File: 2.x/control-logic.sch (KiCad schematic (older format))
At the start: 37 parts, among them P7 SWD, P8 FTDI_SERIAL, SW1 DIPS_08, SW2 RESET, SW3 BOOTLOADER, U2 74HC595, U3 74HC595, U4 LPC11C22FBD48/301, U5 74HC165, X1 12.000 MHz

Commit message: Added RGB output and finished power supply monitor schematic, including new current monitor and voltage monitor divider values.
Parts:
- D33: value HEARTBEAT -> LED
- D34: value POWER_GOOD -> LED
- SW2: value RESET -> BUTTON
- SW3: value BOOTLOADER -> BUTTON
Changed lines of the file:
@@
 $Descr USLetter 11000 8500
 encoding utf-8
-Sheet 5 6
-Title ""
+Sheet 5 7
+Title "DIYPinball Base Board"
 Date "17 mar 2014"
-Rev ""
-Comp ""
+Rev "2.0"
+Comp "DIYPinball.ca"
 Comment1 ""
 Comment2 ""
@@
 SOLENOID_LAMP_LAT
 $Comp
-L GND #PWR28
+L GND #PWR29
 U 1 1 5325ACE0
 P 2800 7550
-F 0 "#PWR28" H 2800 7550 30  0001 C CNN
+F 0 "#PWR29" H 2800 7550 30  0001 C CNN
 F 1 "GND" H 2800 7480 30  0001 C CNN
 F 2 "" H 2800 7550 60  0000 C CNN
@@
 $EndComp
 $Comp
-L GND #PWR32
+L GND #PWR33
 U 1 1 5325BA22
 P 7350 7050
-F 0 "#PWR32" H 7350 7050 30  0001 C CNN
+F 0 "#PWR33" H 7350 7050 30  0001 C CNN
 F 1 "GND" H 7350 6980 30  0001 C CNN
 F 2 "" H 7350 7050 60  0000 C CNN
@@
 VSOL_PRECHARGE_PWM
 $Comp
-L GND #PWR29
+L GND #PWR30
 U 1 1 53262BD9
 P 3650 4200
-F 0 "#PWR29" H 3650 4200 30  0001 C CNN
+F 0 "#PWR30" H 3650 4200 30  0001 C CNN
 F 1 "GND" H 3650 4130 30  0001 C CNN
 F 2 "" H 3650 4200 60  0000 C CNN
@@
 $EndComp
 $Comp
-L GND #PWR31
+L GND #PWR32
 U 1 1 53267486
 P 5350 7850
-F 0 "#PWR31" H 5350 7850 30  0001 C CNN
+F 0 "#PWR32" H 5350 7850 30  0001 C CNN
 F 1 "GND" H 5350 7780 30  0001 C CNN
 F 2 "" H 5350 7850 60  0000 C CNN
@@
 P 8050 2400
 F 0 "SW2" H 8200 2510 50  0000 C CNN
-F 1 "RESET" H 8050 2320 50  0000 C CNN
+F 1 "BUTTON" H 8050 2320 50  0000 C CNN
 F 2 "~" H 8050 2400 60  0000 C CNN
 F 3 "~" H 8050 2400 60  0000 C CNN
@@
 P 8500 2400
 F 0 "SW3" H 8650 2510 50  0000 C CNN
-F 1 "BOOTLOADER" H 8500 2320 50  0000 C CNN
+F 1 "BUTTON" H 8500 2320 50  0000 C CNN
 F 2 "~" H 8500 2400 60  0000 C CNN
 F 3 "~" H 8500 2400 60  0000 C CNN
@@
 P 10100 1900
 F 0 "D34" H 10100 2000 50  0000 C CNN
-F 1 "POWER_GOOD" H 10100 1800 50  0000 C CNN
+F 1 "LED" H 10100 1800 50  0000 C CNN
 F 2 "~" H 10100 1900 60  0000 C CNN
 F 3 "~" H 10100 1900 60  0000 C CNN
@@
 P 9800 1900
 F 0 "D33" H 9800 2000 50  0000 C CNN
-F 1 "HEARTBEAT" H 9800 1800 50  0000 C CNN
+F 1 "LED" H 9800 1800 50  0000 C CNN
 F 2 "~" H 9800 1900 60  0000 C CNN
 F 3 "~" H 9800 1900 60  0000 C CNN
@@
 $EndComp
 $Comp
-L GND #PWR30
+L GND #PWR31
 U 1 1 53268402
 P 4150 4700
-F 0 "#PWR30" H 4150 4700 30  0001 C CNN
+F 0 "#PWR31" H 4150 4700 30  0001 C CNN
 F 1 "GND" H 4150 4630 30  0001 C CNN
 F 2 "" H 4150 4700 60  0000 C CNN
@@
 LOCAL_3V3
 $Comp
-L GND #PWR34
+L GND #PWR35
 U 1 1 53268FE5
 P 8050 2900
-F 0 "#PWR34" H 8050 2900 30  0001 C CNN
+F 0 "#PWR35" H 8050 2900 30  0001 C CNN
 F 1 "GND" H 8050 2830 30  0001 C CNN
 F 2 "" H 8050 2900 60  0000 C CNN
@@
 LOCAL_3V3
 $Comp
-L GND #PWR35
+L GND #PWR36
 U 1 1 532697A4
 P 9950 2900
-F 0 "#PWR35" H 9950 2900 30  0001 C CNN
+F 0 "#PWR36" H 9950 2900 30  0001 C CNN
 F 1 "GND" H 9950 2830 30  0001 C CNN
 F 2 "" H 9950 2900 60  0000 C CNN
@@
 POWER_GOOD
 $Comp
-L GND #PWR33
+L GND #PWR34
 U 1 1 5326A151
 P 7850 3750
-F 0 "#PWR33" H 7850 3750 30  0001 C CNN
+F 0 "#PWR34" H 7850 3750 30  0001 C CNN
 F 1 "GND" H 7850 3680 30  0001 C CNN
 F 2 "" H 7850 3750 60  0000 C CNN
@@
 TXD
 $Comp
-L GND #PWR36
+L GND #PWR37
 U 1 1 5326B790
 P 10000 3750
-F 0 "#PWR36" H 10000 3750 30  0001 C CNN
+F 0 "#PWR37" H 10000 3750 30  0001 C CNN
 F 1 "GND" H 10000 3680 30  0001 C CNN
 F 2 "" H 10000 3750 60  0000 C CNN
@@
 $EndComp
 $Comp
-L GND #PWR?
+L GND #PWR28
 U 1 1 53272581
 P 2800 6150
-F 0 "#PWR?" H 2800 6150 30  0001 C CNN
+F 0 "#PWR28" H 2800 6150 30  0001 C CNN
 F 1 "GND" H 2800 6080 30  0001 C CNN
 F 2 "" H 2800 6150 60  0000 C CNN

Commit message: Adding I2C connector and reannotating to reflect that
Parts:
- added P9: CONN_4, symbol CONN_4
- added R139, R140: 4K7, ~, symbol R
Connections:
- wire segments 198 -> 208
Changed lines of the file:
@@
 Sheet 5 7
 Title "DIYPinball Base Board"
-Date "17 mar 2014"
+Date "2 apr 2014"
 Rev "2.0"
 Comp "DIYPinball.ca"
@@
 LOCAL_3V3
 $Comp
-L GND #PWR36
+L GND #PWR37
 U 1 1 532697A4
 P 9950 2900
-F 0 "#PWR36" H 9950 2900 30  0001 C CNN
+F 0 "#PWR37" H 9950 2900 30  0001 C CNN
 F 1 "GND" H 9950 2830 30  0001 C CNN
 F 2 "" H 9950 2900 60  0000 C CNN
@@
 TXD
 $Comp
-L GND #PWR37
+L GND #PWR38
 U 1 1 5326B790
 P 10000 3750
-F 0 "#PWR37" H 10000 3750 30  0001 C CNN
+F 0 "#PWR38" H 10000 3750 30  0001 C CNN
 F 1 "GND" H 10000 3680 30  0001 C CNN
 F 2 "" H 10000 3750 60  0000 C CNN
@@
 Wire Wire Line
 	1500 2950 2550 2950
+$Comp
+L CONN_4 P9
+U 1 1 533CA25E
+P 9550 4550
+F 0 "P9" V 9500 4550 50  0000 C CNN
+F 1 "CONN_4" V 9600 4550 50  0000 C CNN
+F 2 "" H 9550 4550 60  0000 C CNN
+F 3 "" H 9550 4550 60  0000 C CNN
+	1    9550 4550
+	1    0    0    -1
+$EndComp
+Text Label 8400 4000 0    60   ~ 0
+LOCAL_3V3
+Text Label 8400 4600 0    60   ~ 0
+SCL
+Text Label 8400 4700 0    60   ~ 0
+SDA
+Wire Wire Line
+	8400 4700 9200 4700
+Wire Wire Line
+	9200 4600 8400 4600
+Wire Wire Line
+	8400 4000 9200 4000
+$Comp
+L GND #PWR36
+U 1 1 533CA56F
+P 9100 4800
+F 0 "#PWR36" H 9100 4800 30  0001 C CNN
+F 1 "GND" H 9100 4730 30  0001 C CNN
+F 2 "" H 9100 4800 60  0000 C CNN
+F 3 "" H 9100 4800 60  0000 C CNN
+	1    9100 4800
+	1    0    0    -1
+$EndComp
+Wire Wire Line
+	9100 4800 9100 4500
+Wire Wire Line
+	9100 4500 9200 4500
+Wire Wire Line
+	9200 4000 9200 4400
+$Comp
+L R R140
+U 1 1 533CAC4E
+P 8950 4300
+F 0 "R140" V 9030 4300 40  0000 C CNN
+F 1 "4K7" V 8957 4301 40  0000 C CNN
+F 2 "~" V 8880 4300 30  0000 C CNN
+F 3 "~" H 8950 4300 30  0000 C CNN
+	1    8950 4300
+	1    0    0    -1
+$EndComp
+$Comp
+L R R139
+U 1 1 533CAE0E
+P 8750 4300
+F 0 "R139" V 8830 4300 40  0000 C CNN
+F 1 "4K7" V 8757 4301 40  0000 C CNN
+F 2 "~" V 8680 4300 30  0000 C CNN
+F 3 "~" H 8750 4300 30  0000 C CNN
+	1    8750 4300
+	1    0    0    -1
+$EndComp
+Wire Wire Line
+	8750 4550 8750 4600
+Connection ~ 8750 4600
+Wire Wire Line
+	8950 4550 8950 4700
+Connection ~ 8950 4700
+Wire Wire Line
+	8950 4050 8950 4000
+Connection ~ 8950 4000
+Wire Wire Line
+	8750 4050 8750 4000
+Connection ~ 8750 4000
 $EndSCHEMATC

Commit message: Cleaning up schematic Updating solenoid driver to use 12V for MOSFET gates instead of Vsol so we never exceed Vgs_max
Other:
- moved on the sheet: C10, C12, C14, D33, D34, P8, P9, R103, R104, R105, R106, R107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

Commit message: Started layout on 2.0
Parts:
- removed C10, C13, C14: 100n, ~, symbol C
- removed P7: SWD, symbol CONN_5X2
- removed R101, R102: 10K, ~, symbol R
- removed U2, U3: 74HC595, ~, symbol 74HC595
- removed U4: LPC11C22FBD48/301, symbol LPC11C22FBD48/301
- removed U5: 74HC165, ~, symbol 74LS165
- added C11: 100n, Capacitors_SMD:C_0603, symbol C
- added PGM1: ARM-SWD-HEADER, Myelin:pin_array_5x2_50mil_smd, symbol ARM-SWD-HEADER
- added U2: STM32F072R, Housings_QFP:LQFP-64_10x10mm_Pitch0.5mm, symbol STM32F072R
- added U3: MCP2562, Housings_SOIC:SOIC-8_3.9x4.9mm_Pitch1.27mm, symbol MCP2562
- ADR1: renamed from SW1; footprint (none) -> PinballParts:DIPSWITCH-SMT-08
- BOOT1: renamed from SW3; footprint ~ -> Buttons_Switches_ThroughHole:SW_PUSH_SMALL
- C10: renamed from C11; footprint ~ -> Capacitors_SMD:C_0603
- C12, C4, C5, C6, C7, C8, C9: footprint ~ -> Capacitors_SMD:C_0603
- HB1: renamed from D33; footprint ~ -> LEDs:LED-0603
- I2C1: renamed from P9; footprint (none) -> Sockets_MOLEX_KK-System:Socket_MOLEX-KK-RM2-54mm_Lock_4pin_straight
- PG1: renamed from D34; footprint ~ -> LEDs:LED-0603
- R101: renamed from R111; footprint ~ -> Resistors_SMD:R_0603
- R102: renamed from R112; footprint ~ -> Resistors_SMD:R_0603
- R103: renamed from R113; footprint ~ -> Resistors_SMD:R_0603
- R104: renamed from R114; footprint ~ -> Resistors_SMD:R_0603
- R105: renamed from R139; value 4K7 -> 4.7K; footprint ~ -> Resistors_SMD:R_0603
- R106: renamed from R140; value 4K7 -> 4.7K; footprint ~ -> Resistors_SMD:R_0603
- R107: renamed from R103; footprint ~ -> Resistors_SMD:R_0603
- R108: renamed from R104; footprint ~ -> Resistors_SMD:R_0603
- R109: renamed from R105; footprint ~ -> Resistors_SMD:R_0603
- R110: renamed from R106; footprint ~ -> Resistors_SMD:R_0603
- R111: renamed from R107; footprint ~ -> Resistors_SMD:R_0603
- R112: renamed from R108; footprint ~ -> Resistors_SMD:R_0603
- R113: renamed from R109; footprint ~ -> Resistors_SMD:R_0603
- R114: renamed from R110; footprint ~ -> Resistors_SMD:R_0603
- RESET1: renamed from SW2; footprint ~ -> Buttons_Switches_ThroughHole:SW_PUSH_SMALL
- SERIAL1: renamed from P8; footprint (none) -> Socket_Strips:Socket_Strip_Straight_1x06
- X1: value 12.000 MHz -> 8.000 MHz; footprint ~ -> Crystals_Oscillators_SMD:Q_49U3HMS
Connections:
- net labels added: ADDRESS0, ADDRESS1, ADDRESS2, ADDRESS3, ADDRESS4, ADDRESS5, ADDRESS6, ADDRESS7, CANRX, CANTX, ~RESET
- net labels removed: DIP_CLK, DIP_DAT, DIP_LAT, RESET, SOLENOID_LAMP_CLEAR, SOLENOID_LAMP_CLK, SOLENOID_LAMP_DAT, SOLENOID_LAMP_LAT
- wire segments 208 -> 188
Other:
- moved on the sheet: ADR1, C10, C4, C5, C6, C7, C8, C9, R107, R108, R109, R110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

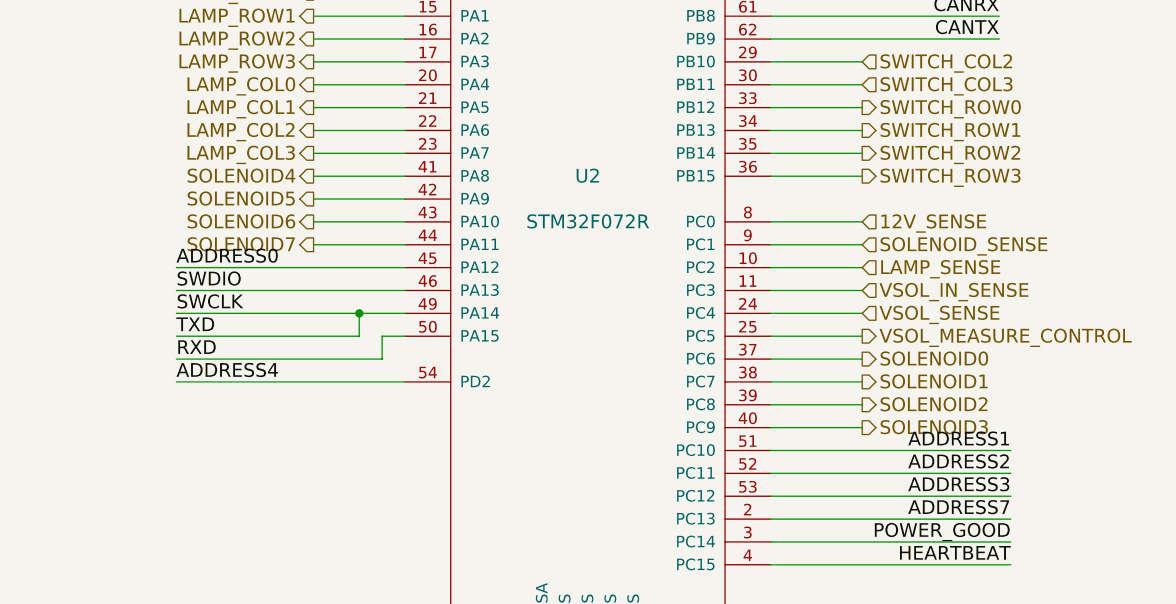
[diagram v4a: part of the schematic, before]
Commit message: 2.0 is getting very close. Adjusted the solenoid connections to allow a cleaner layout.
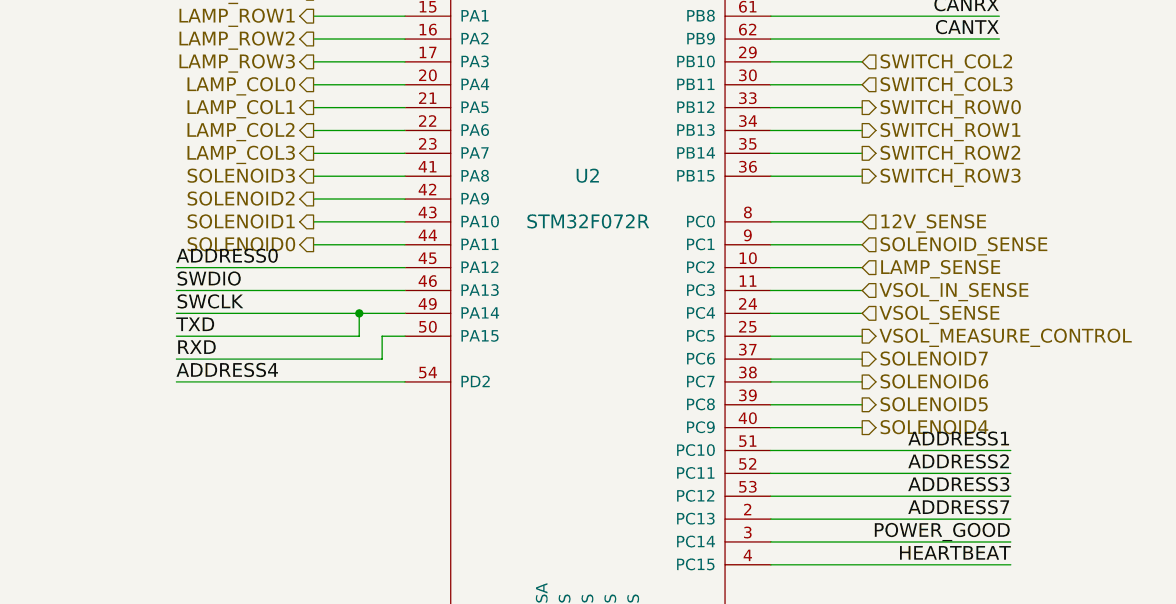
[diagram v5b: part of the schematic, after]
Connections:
- net SOLENOID0: now also U2.44 (PA11); no longer U2.37 (PC6)
- net SOLENOID1: now also U2.43 (PA10); no longer U2.38 (PC7)
- net SOLENOID2: now also U2.42 (PA9); no longer U2.39 (PC8)
- net SOLENOID3: now also U2.41 (PA8); no longer U2.40 (PC9)
- net SOLENOID4: now also U2.40 (PC9); no longer U2.41 (PA8)
- net SOLENOID5: now also U2.39 (PC8); no longer U2.42 (PA9)
- net SOLENOID6: now also U2.38 (PC7); no longer U2.43 (PA10)
- net SOLENOID7: now also U2.37 (PC6); no longer U2.44 (PA11)
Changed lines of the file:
@@
 Comment4 ""
 $EndDescr
+Text HLabel 2050 3500 0    60   Output ~ 0
+SOLENOID0
+Text HLabel 2050 3400 0    60   Output ~ 0
+SOLENOID1
+Text HLabel 2050 3300 0    60   Output ~ 0
+SOLENOID2
+Text HLabel 2050 3200 0    60   Output ~ 0
+SOLENOID3
+Text HLabel 4450 4300 2    60   Output ~ 0
+SOLENOID4
+Text HLabel 4450 4200 2    60   Output ~ 0
+SOLENOID5
+Text HLabel 4450 4100 2    60   Output ~ 0
+SOLENOID6
 Text HLabel 4450 4000 2    60   Output ~ 0
-SOLENOID0
-Text HLabel 4450 4100 2    60   Output ~ 0
-SOLENOID1
-Text HLabel 4450 4200 2    60   Output ~ 0
-SOLENOID2
-Text HLabel 4450 4300 2    60   Output ~ 0
-SOLENOID3
-Text HLabel 2050 3200 0    60   Output ~ 0
-SOLENOID4
-Text HLabel 2050 3300 0    60   Output ~ 0
-SOLENOID5
-Text HLabel 2050 3400 0    60   Output ~ 0
-SOLENOID6
-Text HLabel 2050 3500 0    60   Output ~ 0
 SOLENOID7
 Text HLabel 2050 2400 0    60   Output ~ 0
@@
 SCL
 Wire Wire Line
-	4050 4000 4450 4000
-Wire Wire Line
-	4450 4100 4050 4100
-Wire Wire Line
-	4050 4200 4450 4200
-Wire Wire Line
-	4450 4300 4050 4300
-Wire Wire Line
-	2450 3200 2050 3200
-Wire Wire Line
-	2050 3300 2450 3300
-Wire Wire Line
-	2450 3400 2050 3400
-Wire Wire Line
-	2050 3500 2450 3500
-Wire Wire Line
 	2050 3100 2450 3100
 Wire Wire Line
@@
 Wire Wire Line
 	2450 2600 2050 2600
+Wire Wire Line
+	4450 4000 4050 4000
+Wire Wire Line
+	4050 4100 4450 4100
+Wire Wire Line
+	4450 4200 4050 4200
+Wire Wire Line
+	4050 4300 4450 4300
+Wire Wire Line
+	2450 3500 2050 3500
+Wire Wire Line
+	2050 3400 2450 3400
+Wire Wire Line
+	2050 3200 2450 3200
+Wire Wire Line
+	2450 3300 2050 3300
 $EndSCHEMATC

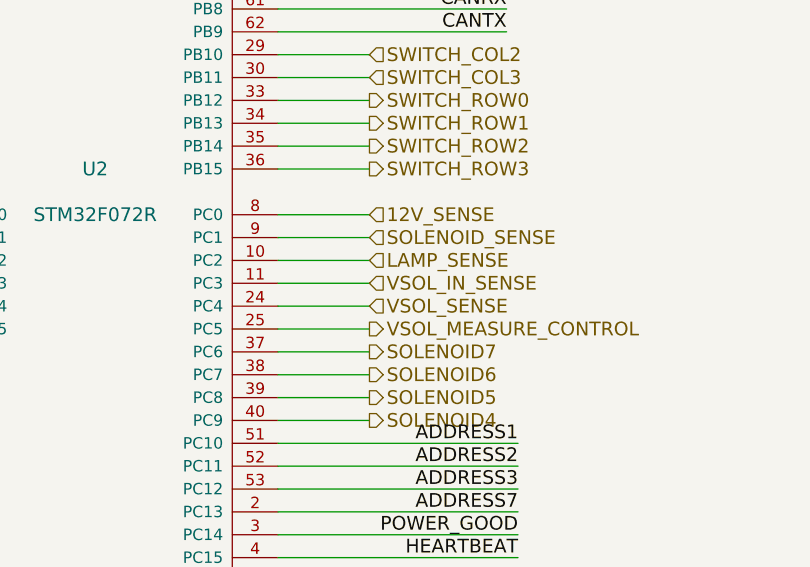
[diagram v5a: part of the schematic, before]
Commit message: Power layers set up. A few footprint/pinout changes and some silkscreen cleanup, and the first rev is complete.
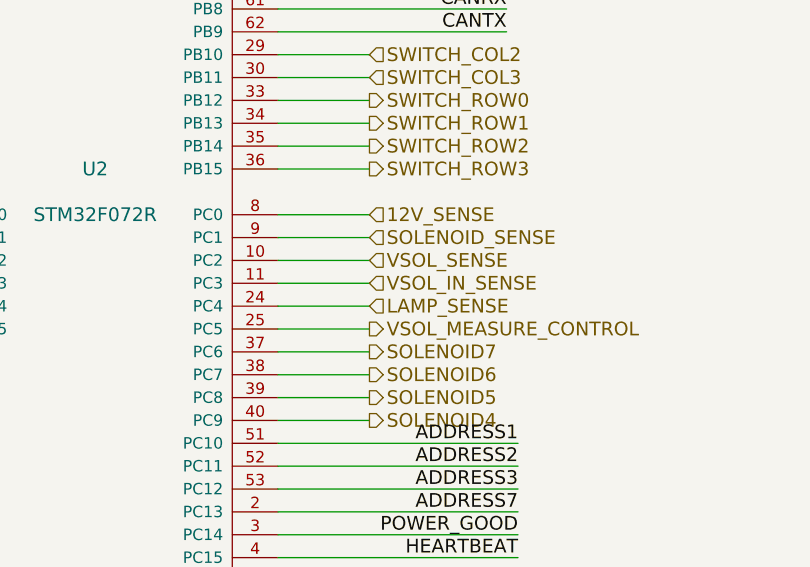
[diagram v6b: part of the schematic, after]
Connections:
- net LAMP_SENSE: now also U2.24 (PC4); no longer U2.10 (PC2)
- net VSOL_SENSE: now also U2.10 (PC2); no longer U2.24 (PC4)
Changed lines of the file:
@@
 Text HLabel 4450 3500 2    60   Input ~ 0
 SOLENOID_SENSE
-Text HLabel 4450 3600 2    60   Input ~ 0
+Text HLabel 4450 3800 2    60   Input ~ 0
 LAMP_SENSE
 Text HLabel 2850 1000 0    60   Input ~ 0
@@
 	1    0    0    -1
 $EndComp
-Text HLabel 4450 3800 2    60   Input ~ 0
+Text HLabel 4450 3600 2    60   Input ~ 0
 VSOL_SENSE
 Text HLabel 4450 3900 2    60   Output ~ 0
@@
 	4450 3900 4050 3900
 Wire Wire Line
-	4450 3800 4050 3800
-Wire Wire Line
 	4450 3700 4050 3700
 Wire Wire Line
 	4450 3400 4050 3400
-Wire Wire Line
-	4450 3600 4050 3600
 Wire Wire Line
 	4450 3500 4050 3500
@@
 Wire Wire Line
 	2450 3300 2050 3300
+Wire Wire Line
+	4450 3600 4050 3600
+Wire Wire Line
+	4050 3800 4450 3800
 $EndSCHEMATC

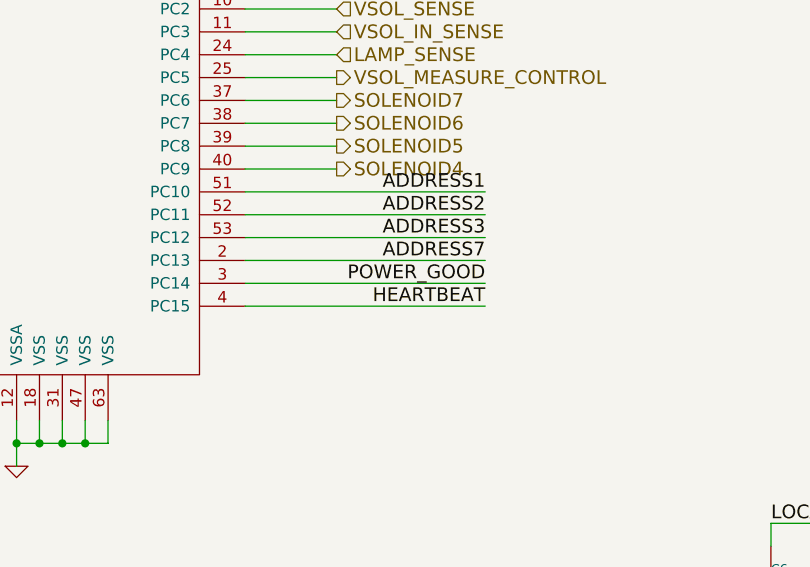
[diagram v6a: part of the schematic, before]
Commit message: Finishing layout updates from review with Mike.
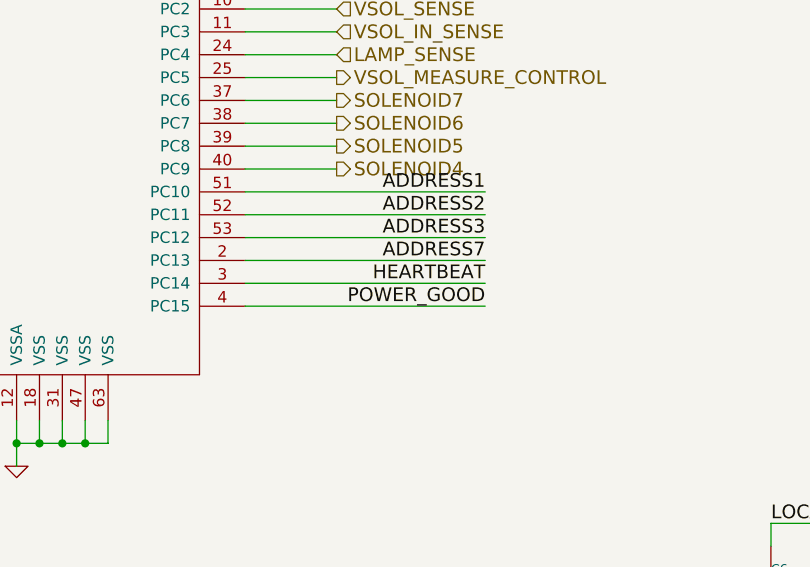
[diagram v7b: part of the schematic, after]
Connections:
- net HEARTBEAT: now also U2.3 (PC14); no longer U2.4 (PC15)
- net POWER_GOOD: now also U2.4 (PC15); no longer U2.3 (PC14)
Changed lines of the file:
@@
 $EndComp
 Text Label 5100 4900 2    60   ~ 0
+POWER_GOOD
+Text Label 5100 4800 2    60   ~ 0
 HEARTBEAT
-Text Label 5100 4800 2    60   ~ 0
-POWER_GOOD
 Text Label 4050 1100 2    60   ~ 0
 LOCAL_3V3
